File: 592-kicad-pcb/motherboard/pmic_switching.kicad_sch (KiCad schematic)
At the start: 10 parts, among them U23 ISL54059IRUZ-T, U25 ISL54059IRUZ-T, U26 INA138NA/3K, U27 INA138NA/3K, U36 ISL54059IRUZ-T

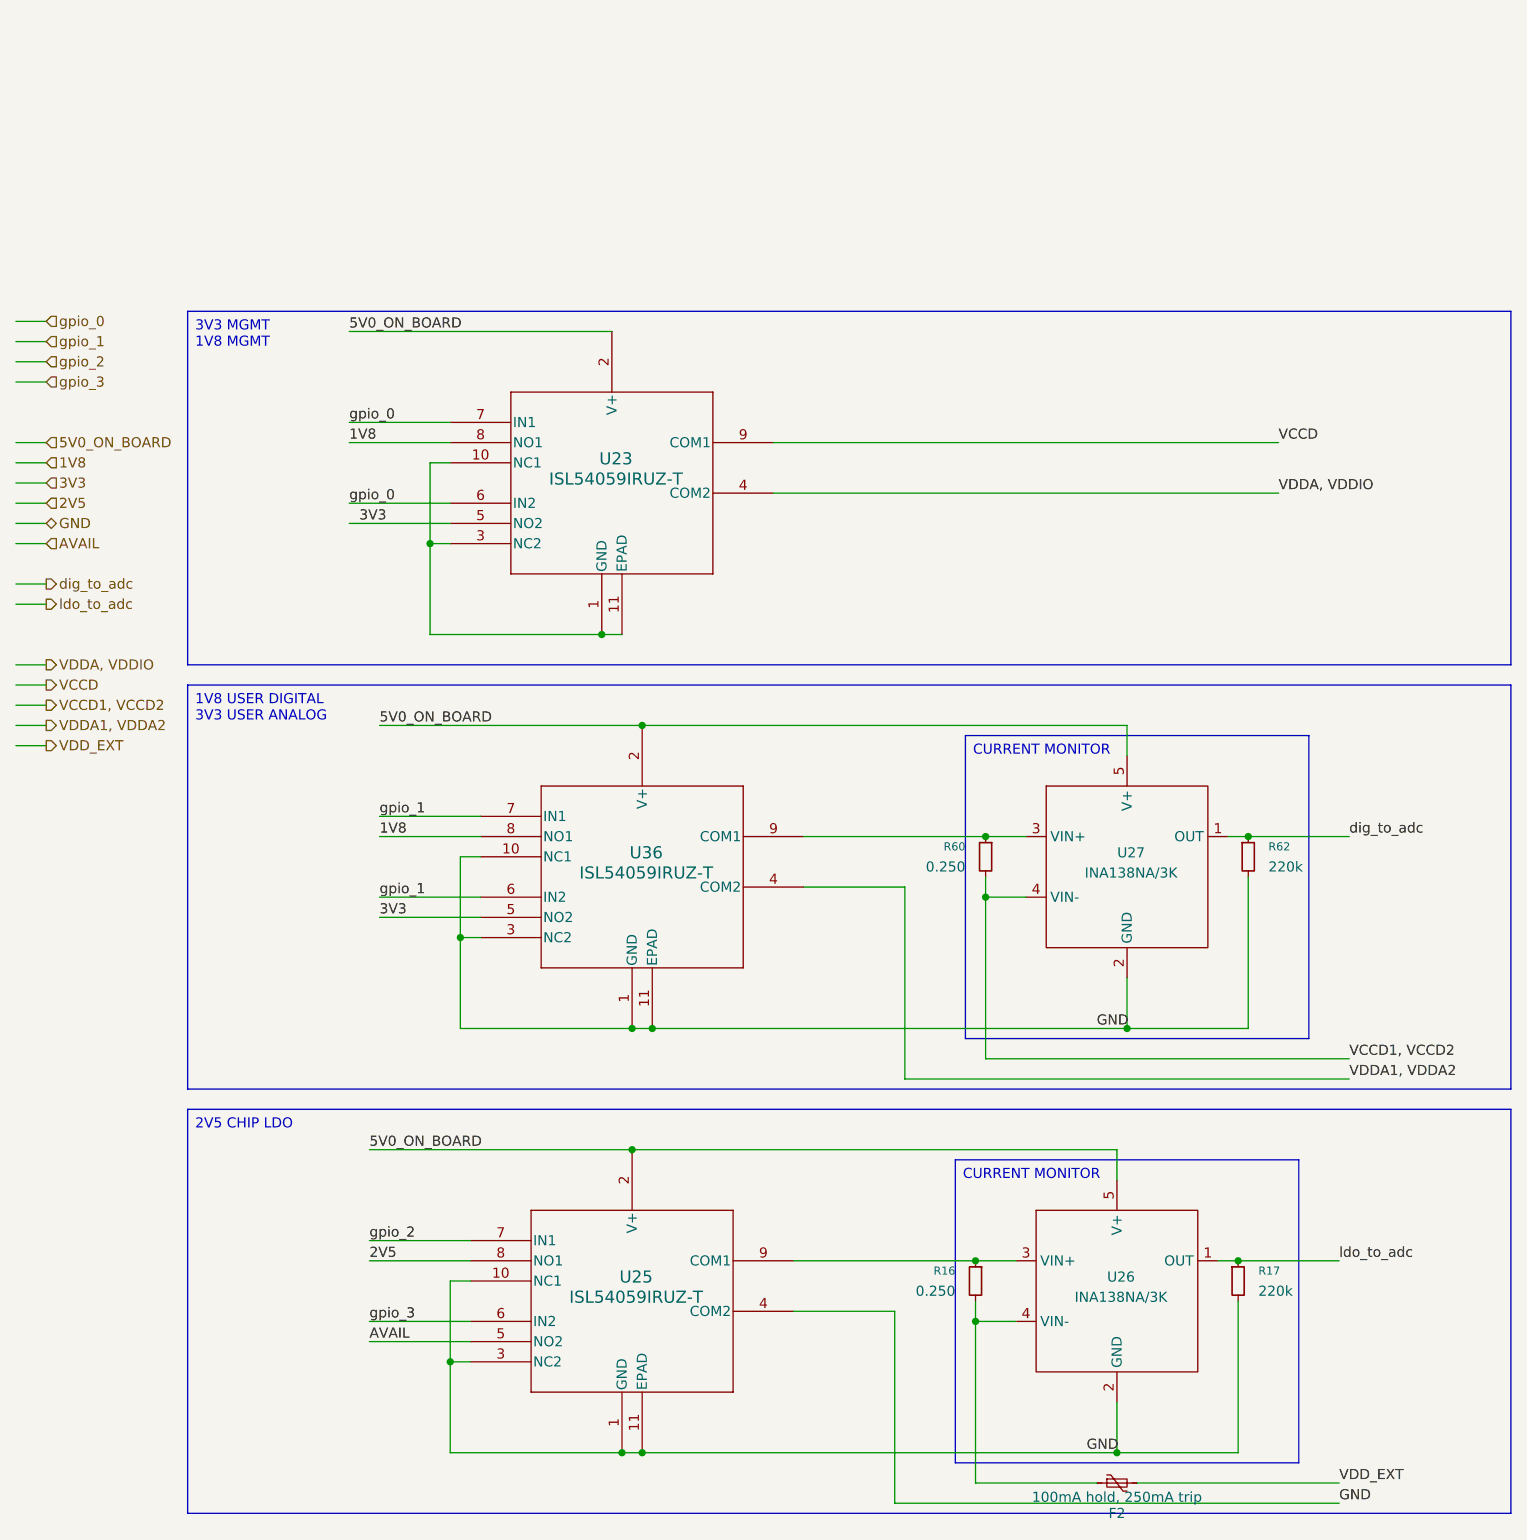
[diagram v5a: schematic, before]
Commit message: no erc errors but on root
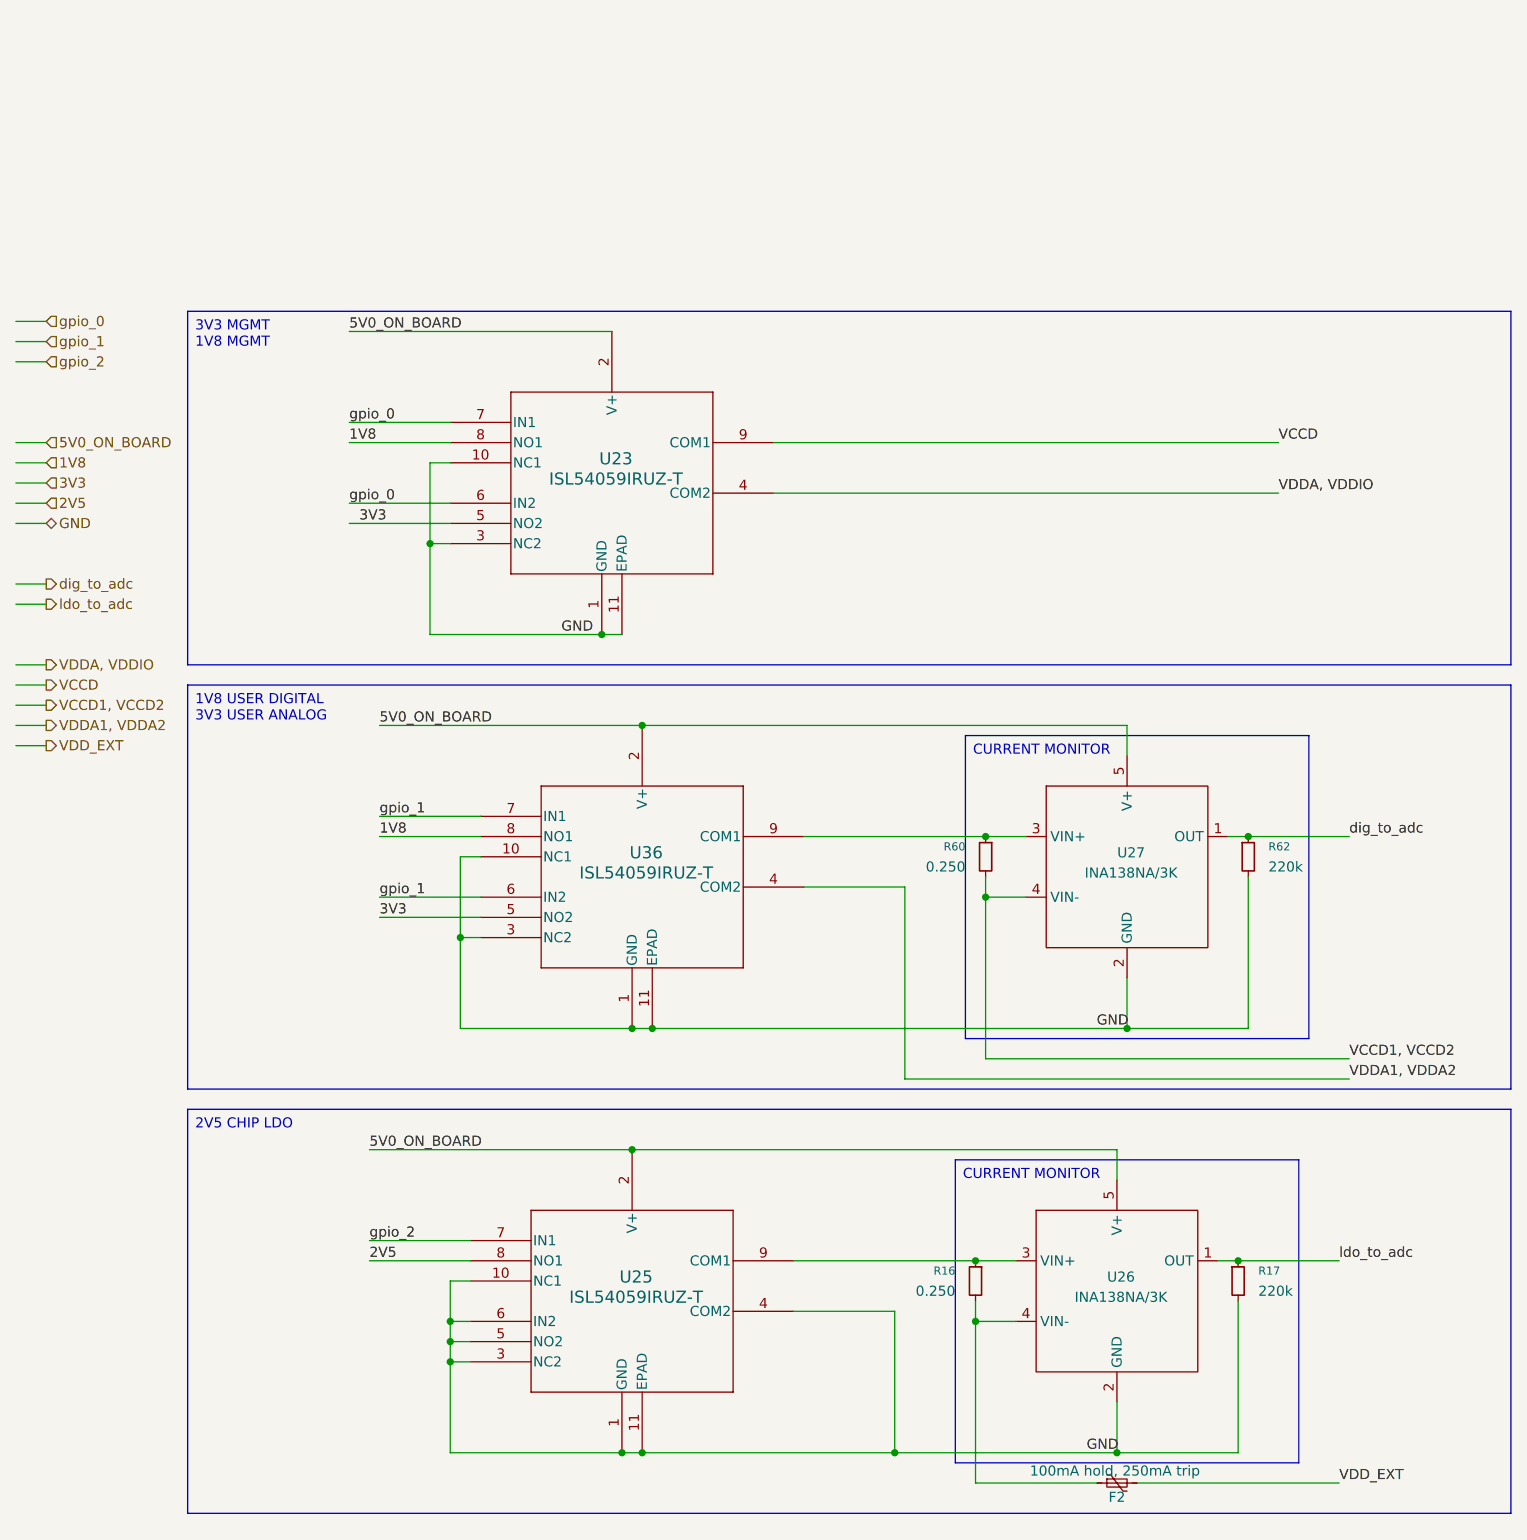
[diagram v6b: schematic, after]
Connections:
- net AVAIL is gone; now on net GND: U25.5 (NO2)
- net gpio_3 is gone; now on net GND: U25.6 (IN2)
- net GND: now also U23.1 (GND), U23.10 (NC1), U23.11 (EPAD), U23.3 (NC2)
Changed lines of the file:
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@@
+	)
+	(junction
+		(at 71.12 140.97)
+		(diameter 0)
+		(color 0 0 0 0)
 	)
 	(junction
@@
 	)
 	(junction
+		(at 71.12 143.51)
+		(diameter 0)
+		(color 0 0 0 0)
+	)
+	(junction
 		(at 156.21 104.14)
 		(diameter 0)
@@
 	)
 	(junction
+		(at 127 157.48)
+		(diameter 0)
+		(color 0 0 0 0)
+	)
+	(junction
 		(at 137.16 133.35)
 		(diameter 0)
@@
 	(wire
 		(pts
-			(xy 16.51 43.18) (xy 20.32 43.18)
-		)
-		(stroke
-			(width 0)
-			(type default)
-		)
-	)
-	(wire
-		(pts
 			(xy 168.91 80.01) (xy 171.45 80.01)
 		)
@@
 	(wire
 		(pts
+			(xy 71.12 140.97) (xy 71.12 135.89)
+		)
+		(stroke
+			(width 0)
+			(type default)
+		)
+	)
+	(wire
+		(pts
 			(xy 16.51 66.04) (xy 20.32 66.04)
 		)
@@
 	(wire
 		(pts
-			(xy 60.96 140.97) (xy 73.66 140.97)
-		)
-		(stroke
-			(width 0)
-			(type default)
-		)
-	)
-	(wire
-		(pts
-			(xy 127 139.7) (xy 114.3 139.7)
-		)
-		(stroke
-			(width 0)
-			(type default)
-		)
-	)
-	(wire
-		(pts
 			(xy 68.58 33.02) (xy 68.58 43.18)
 		)
@@
 	(wire
 		(pts
+			(xy 127 157.48) (xy 154.94 157.48)
+		)
+		(stroke
+			(width 0)
+			(type default)
+		)
+	)
+	(wire
+		(pts
 			(xy 137.16 140.97) (xy 142.24 140.97)
 		)
@@
 	(wire
 		(pts
-			(xy 16.51 22.86) (xy 20.32 22.86)
-		)
-		(stroke
-			(width 0)
-			(type default)
-		)
-	)
-	(wire
-		(pts
 			(xy 95.25 66.04) (xy 156.21 66.04)
 		)
@@
 	(wire
 		(pts
+			(xy 71.12 143.51) (xy 71.12 140.97)
+		)
+		(stroke
+			(width 0)
+			(type default)
+		)
+	)
+	(wire
+		(pts
 			(xy 16.51 15.24) (xy 20.32 15.24)
 		)
@@
 	(wire
 		(pts
+			(xy 71.12 140.97) (xy 73.66 140.97)
+		)
+		(stroke
+			(width 0)
+			(type default)
+		)
+	)
+	(wire
+		(pts
 			(xy 68.58 33.02) (xy 71.12 33.02)
 		)
@@
 	(wire
 		(pts
-			(xy 60.96 143.51) (xy 73.66 143.51)
+			(xy 71.12 143.51) (xy 73.66 143.51)
 		)
 		(stroke
@@
 	(wire
 		(pts
-			(xy 71.12 146.05) (xy 71.12 135.89)
+			(xy 71.12 146.05) (xy 71.12 143.51)
 		)
 		(stroke
@@
 	(wire
 		(pts
+			(xy 127 139.7) (xy 127 157.48)
+		)
+		(stroke
+			(width 0)
+			(type default)
+		)
+	)
+	(wire
+		(pts
 			(xy 138.43 107.95) (xy 184.15 107.95)
 		)
@@
 	(wire
 		(pts
+			(xy 114.3 139.7) (xy 127 139.7)
+		)
+		(stroke
+			(width 0)
+			(type default)
+		)
+	)
+	(wire
+		(pts
 			(xy 16.51 35.56) (xy 20.32 35.56)
 		)
@@
 	(wire
 		(pts
-			(xy 127 163.83) (xy 182.88 163.83)
-		)
-		(stroke
-			(width 0)
-			(type default)
-		)
-	)
-	(wire
-		(pts
 			(xy 92.71 157.48) (xy 95.25 157.48)
 		)
@@
 	(wire
 		(pts
-			(xy 127 139.7) (xy 127 163.83)
-		)
-		(stroke
-			(width 0)
-			(type default)
-		)
-	)
-	(wire
-		(pts
-			(xy 95.25 157.48) (xy 154.94 157.48)
+			(xy 95.25 157.48) (xy 127 157.48)
 		)
 		(stroke
@@
 		)
 	)
+	(label "GND"
+		(at 85.09 54.61 0)
+		(effects
+			(font
+				(size 1.27 1.27)
+			)
+			(justify left bottom)
+		)
+	)
 	(label "VCCD"
 		(at 175.26 30.48 0)
@@
 		)
 	)
-	(label "AVAIL"
-		(at 60.96 143.51 0)
-		(effects
-			(font
-				(size 1.27 1.27)
-			)
-			(justify left bottom)
-		)
-	)
 	(label "1V8"
 		(at 58.42 30.48 0)
@@
 		)
 	)
-	(label "gpio_3"
-		(at 60.96 140.97 0)
-		(effects
-			(font
-				(size 1.27 1.27)
-			)
-			(justify left bottom)
-		)
-	)
 	(label "gpio_1"
 		(at 62.23 87.63 0)
@@
 	(label "VDDA1, VDDA2"
 		(at 184.15 110.49 0)
-		(effects
-			(font
-				(size 1.27 1.27)
-			)
-			(justify left bottom)
-		)
-	)
-	(label "GND"
-		(at 182.88 163.83 0)
 		(effects
 			(font
@@
 		)
 	)
-	(hierarchical_label "gpio_3"
-		(shape input)
-		(at 20.32 22.86 0)
-		(effects
-			(font
-				(size 1.27 1.27)
-			)
-			(justify left)
-		)
-	)
 	(hierarchical_label "VDD_EXT"
 		(shape output)
@@
 		(shape output)
 		(at 20.32 58.42 0)
-		(effects
-			(font
-				(size 1.27 1.27)
-			)
-			(justify left)
-		)
-	)
-	(hierarchical_label "AVAIL"
-		(shape input)
-		(at 20.32 43.18 0)
 		(effects
 			(font
@@
 		(dnp no)
 		(property "Reference" "F2"
-			(at 154.94 165.1 90)
+			(at 154.94 163.068 90)
 			(effects
 				(font
@@
 		)
 		(property "Value" "100mA hold, 250mA trip"
-			(at 154.94 163.068 90)
-			(effects
-				(font
+			(at 154.686 159.766 90)
+			(effects
+				(font
